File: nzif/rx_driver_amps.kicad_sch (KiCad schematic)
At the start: 84 parts, among them U301 LT5400BCMS8E-8-TRPBF, U302 LT5400BCMS8E-8-TRPBF, U303 ADA4945-1, U304 ADG884xCP, U305 ADA4945-1, U306 ADG884xCP, U307 LT5400BCMS8E-8-TRPBF, U308 LT5400BCMS8E-8-TRPBF, U309 ADG884xCP, U310 ADG884xCP, U311 ADA4945-1, U312 ADA4945-1

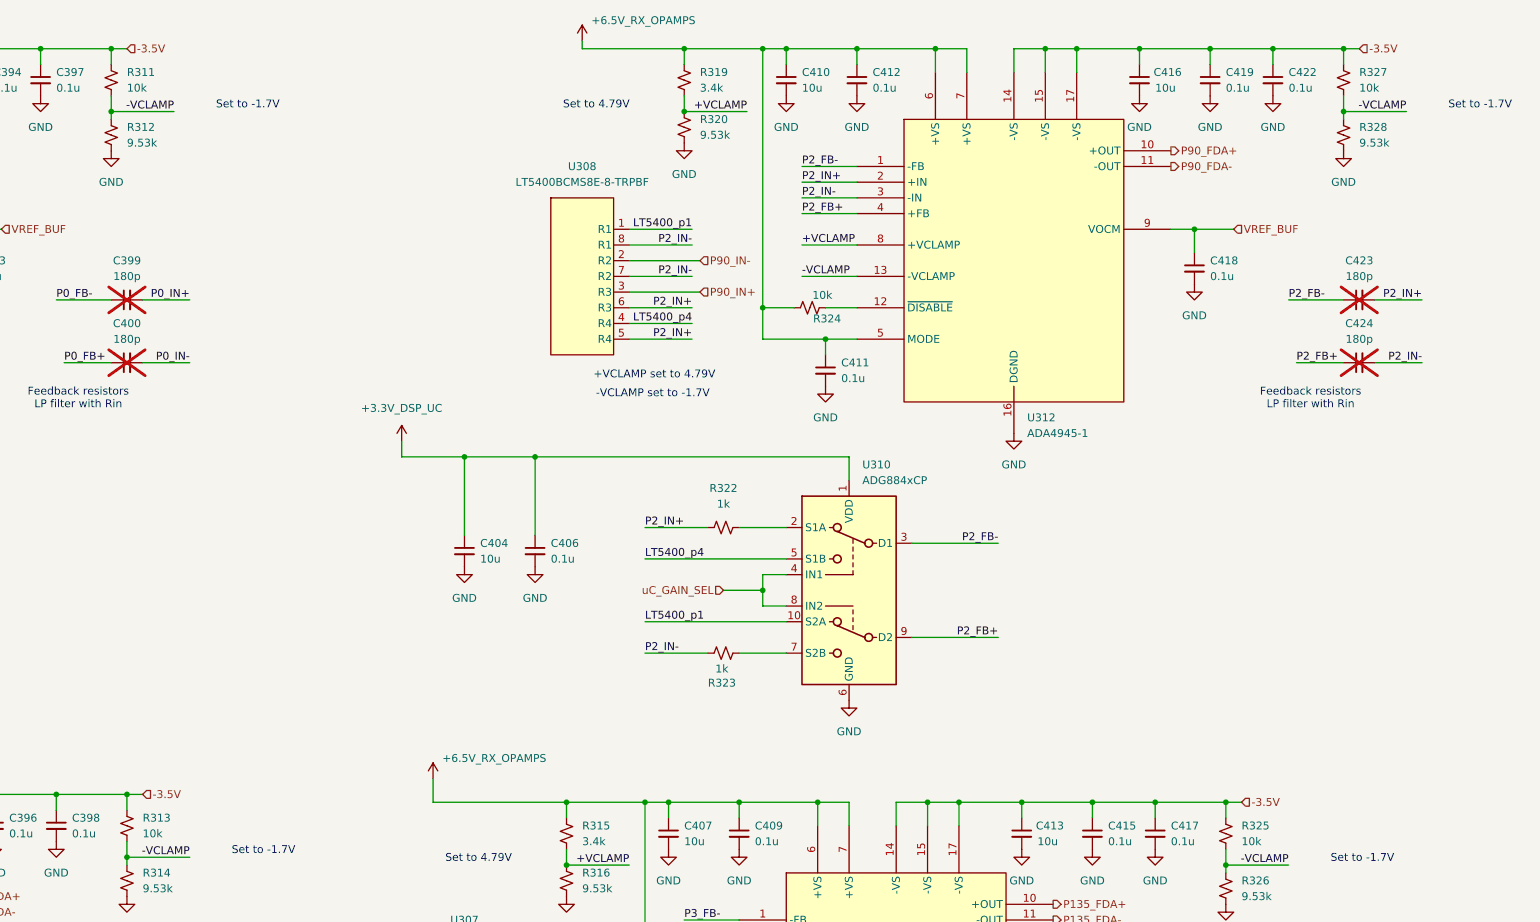
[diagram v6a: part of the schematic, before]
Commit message: added -3.5V rail
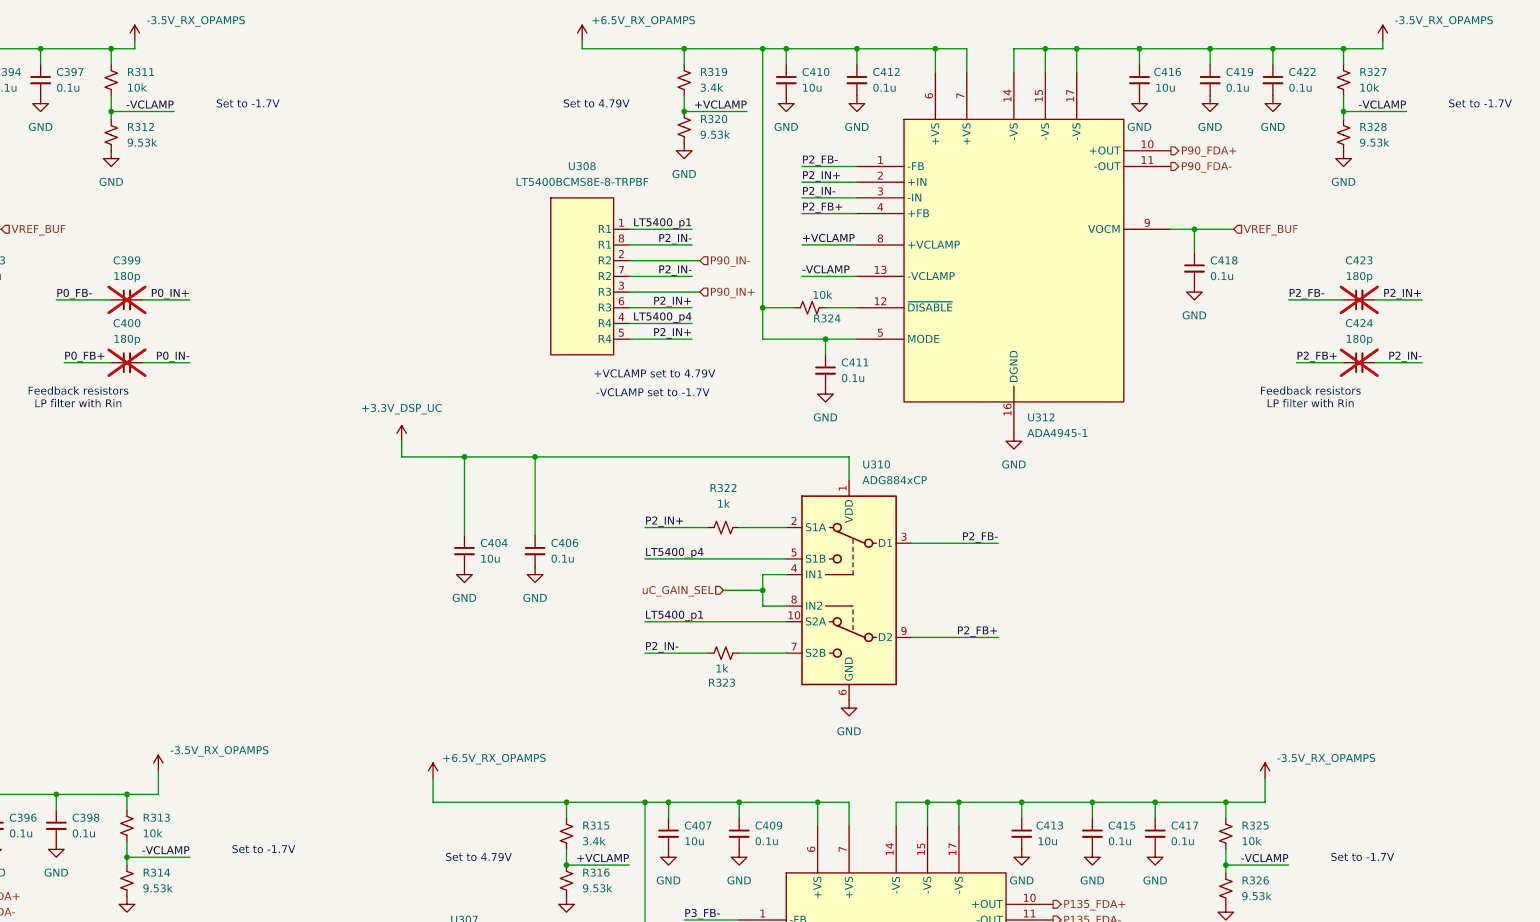
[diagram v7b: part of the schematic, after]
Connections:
- net -3.5V renamed -3.5V_RX_OPAMPS
